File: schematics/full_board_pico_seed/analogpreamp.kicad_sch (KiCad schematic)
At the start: 61 parts, among them J1 XLR3, J3 Aux In, J4 Conn_01x02_Pin, J7 XLR3, J8 XLR3, U1 TL074, U4 NE5534, U9 TL074

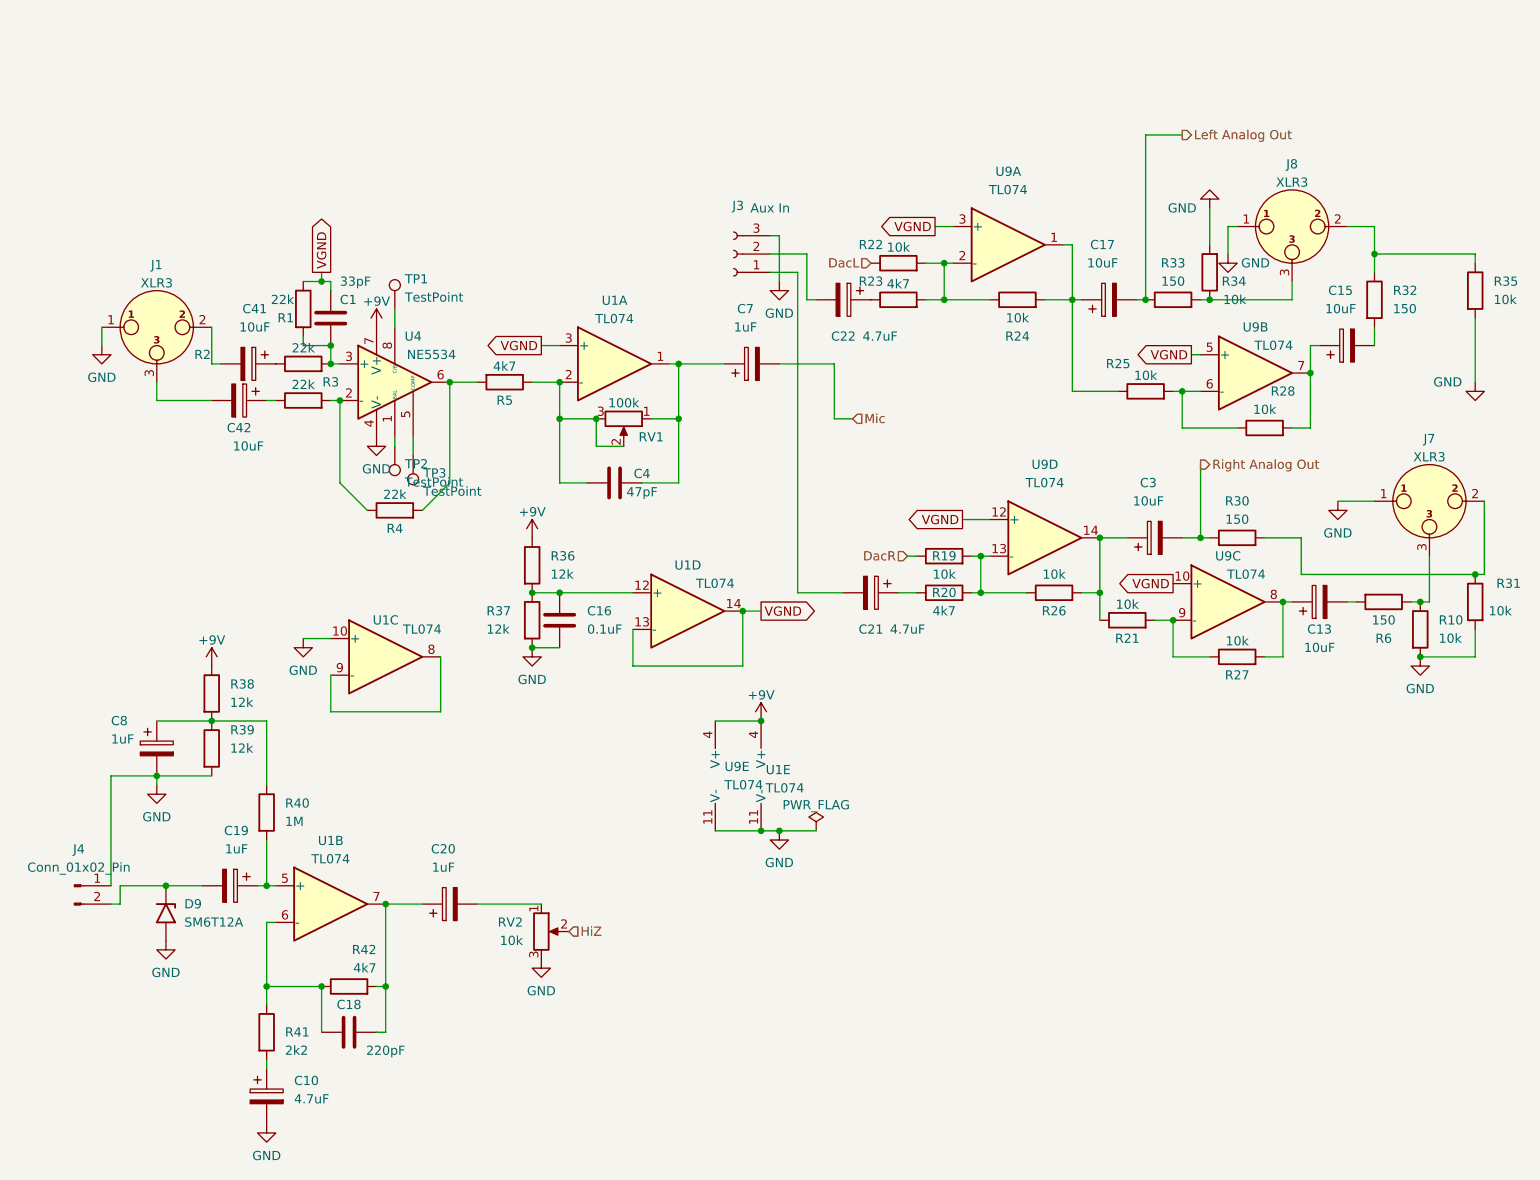
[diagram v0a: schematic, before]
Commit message: more work on full schematic: added test points
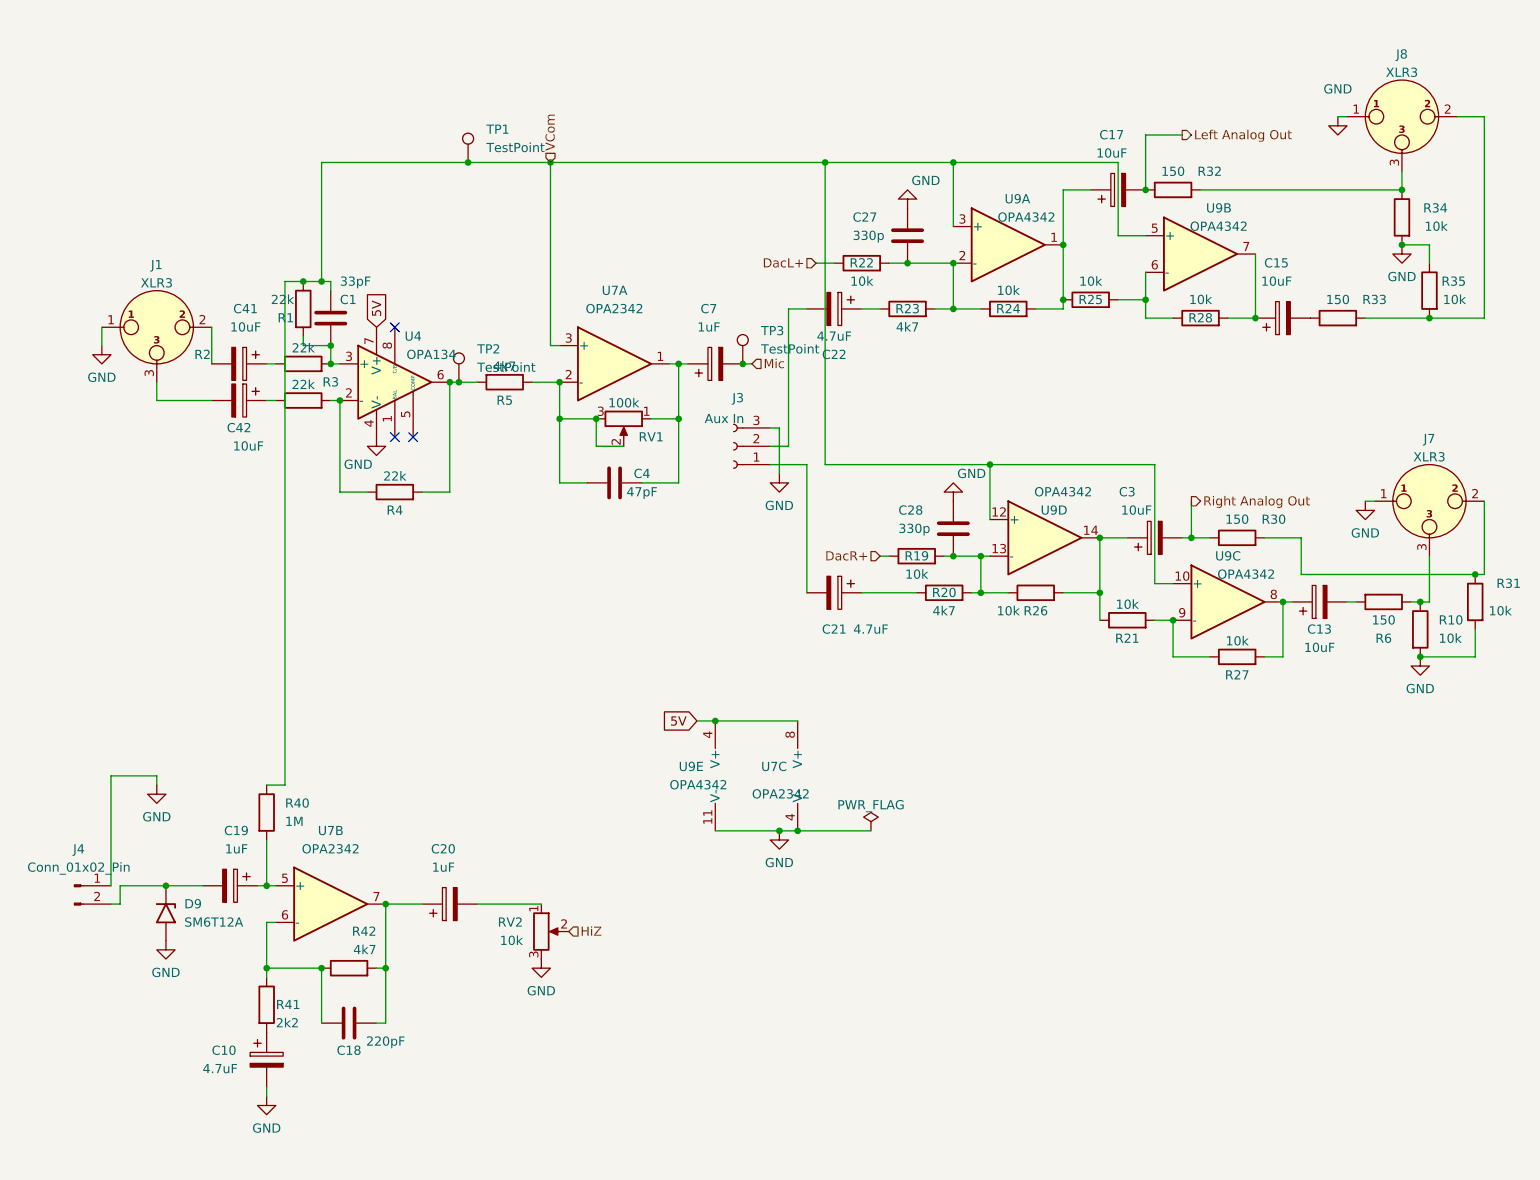
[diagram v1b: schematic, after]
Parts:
- removed C16: 0.1uF, Capacitor_SMD:C_1210_3225Metric_Pad1.33x2.70mm_HandSolder, symbol Device:C
- removed C8: 1uF, Capacitor_SMD:CP_Elec_4x4.5, symbol Device:C_Polarized
- removed R36, R37, R38, R39: 12k, Resistor_SMD:R_0603_1608Metric_Pad0.98x0.95mm_HandSolder, symbol Device:R
- removed U1: TL074, Package_SO:SOIC-14_3.9x8.7mm_P1.27mm, symbol Amplifier_Operational:TL074
- added C27, C28: 330p, Capacitor_SMD:C_0603_1608Metric_Pad1.08x0.95mm_HandSolder, symbol Device:C
- added U7: OPA2342, Package_SO:SOIC-8_3.9x4.9mm_P1.27mm, symbol Amplifier_Operational:TL072
- U4: value NE5534 -> OPA134
- U9: value TL074 -> OPA4342
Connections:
- net VGND is gone; now on net VCom: C1.1, R1.1, U9.10 (+), U9.12 (+), U9.3 (+), U9.5 (+)
- net GND: now also R35.1, C27.1, C28.1, U7.4 (V-); no longer R35.2
- net Left Analog Out: now also R32.1; no longer R33.1
- net Mic: now also TP3.1
- net at U4.1 (BAL): no longer TP2.1
- net at U4.5 (COMP): no longer TP3.1
- net at R4.2, R5.2, U4.6: now also TP2.1
- net at U4.8 (C/B): no longer TP1.1
- net at R19.2, R20.2, R26.1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: now also C28.2
- net at J8.3, R34.1: now also R32.2; no longer R33.2
- net at C4.2, C7.1, RV1.1: now also U7.1
- net at R22.2, R23.2, R24.1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: now also C27.2
- net at C4.1, R5.1, RV1.2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: now also U7.2 (-)
- net at C15.2: now also R33.1; no longer R32.2
- net VCom: now reaches R40.1
- net VCom: now also TP1.1, U7.3 (+)
- net at C18.1, R41.1, R42.1: now also U7.6 (-)
- net at C19.1, R40.2: now also U7.5 (+)
- net at C18.2, C20.1, R42.2: now also U7.7
- net +9V renamed 5V
- net 5V: now also U7.8 (V+)
- net DacL renamed DacL+
- net DacR renamed DacR+
- new net: J8.2, R33.2, R35.2
- no-connect marks 0 -> 3
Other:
- moved on the sheet: C10, C17, C18, C21, C22, C41, C7, J3, J8, R19, R26, R4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

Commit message: worked on schematics
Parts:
- J1, J3, J4, J7, J8, RV1, RV2, TP1, TP2, TP3: now left out of the parts list
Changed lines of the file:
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@@
 		(shape input)
 		(at 88.9 34.29 90)
-		(fields_autoplaced yes)
 		(effects
 			(font
@@
 		(shape input)
 		(at 134.62 88.9 180)
-		(fields_autoplaced yes)
 		(effects
 			(font
@@
 		(shape input)
 		(at 116.84 62.23 0)
-		(fields_autoplaced yes)
 		(effects
 			(font
@@
 		(shape input)
 		(at 125.73 48.26 180)
-		(fields_autoplaced yes)
 		(effects
 			(font
@@
 		(shape output)
 		(at 177.8 81.28 0)
-		(fields_autoplaced yes)
 		(effects
 			(font
@@
 		(shape output)
 		(at 176.53 30.48 0)
-		(fields_autoplaced yes)
 		(effects
 			(font
@@
 		(shape input)
 		(at 91.44 140.97 0)
-		(fields_autoplaced yes)
 		(effects
 			(font
@@
 		(unit 1)
 		(exclude_from_sim no)
-		(in_bom yes)
+		(in_bom no)
 		(on_board yes)
 		(dnp no)
@@
 			)
 		)
-		(property "Datasheet" " ~"
+		(property "Datasheet" "~"
 			(at 34.29 57.15 0)
 			(effects
@@
 		(unit 1)
 		(exclude_from_sim no)
-		(in_bom yes)
+		(in_bom no)
 		(on_board yes)
 		(dnp no)
@@
 			)
 		)
-		(property "Datasheet" " ~"
+		(property "Datasheet" "~"
 			(at 207.01 27.94 0)
 			(effects
@@
 		(unit 1)
 		(exclude_from_sim no)
-		(in_bom yes)
+		(in_bom no)
 		(on_board yes)
 		(dnp no)
@@
 		(unit 1)
 		(exclude_from_sim no)
-		(in_bom yes)
+		(in_bom no)
 		(on_board yes)
 		(dnp no)
@@
 		(unit 1)
 		(exclude_from_sim no)
-		(in_bom yes)
+		(in_bom no)
 		(on_board yes)
 		(dnp no)
@@
 			)
 		)
-		(property "Datasheet" " ~"
+		(property "Datasheet" "~"
 			(at 210.82 81.28 0)
 			(effects
@@
 		(unit 1)
 		(exclude_from_sim no)
-		(in_bom yes)
+		(in_bom no)
 		(on_board yes)
 		(dnp no)
@@
 		(unit 1)
 		(exclude_from_sim no)
-		(in_bom yes)
+		(in_bom no)
 		(on_board yes)
 		(dnp no)
@@
 		(unit 1)
 		(exclude_from_sim no)
-		(in_bom yes)
+		(in_bom no)
 		(on_board yes)
 		(dnp no)
@@
 		(unit 1)
 		(exclude_from_sim no)
-		(in_bom yes)
+		(in_bom no)
 		(on_board yes)
 		(dnp no)
@@
 		(unit 1)
 		(exclude_from_sim no)
-		(in_bom yes)
+		(in_bom no)
 		(on_board yes)
 		(dnp no)

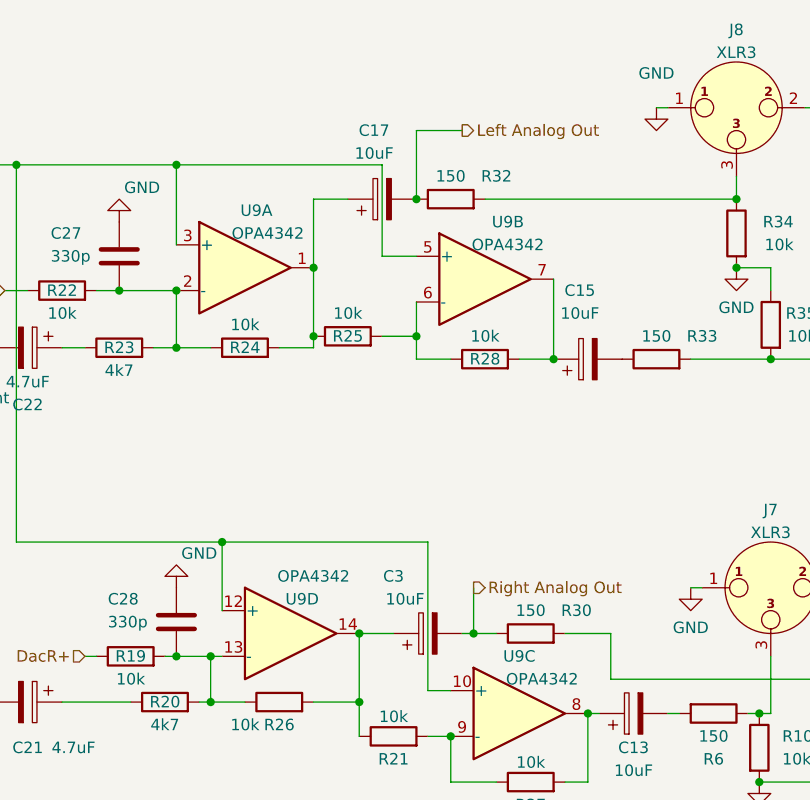
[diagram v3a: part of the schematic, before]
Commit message: corrected wiring mistake found during hw test of first batch
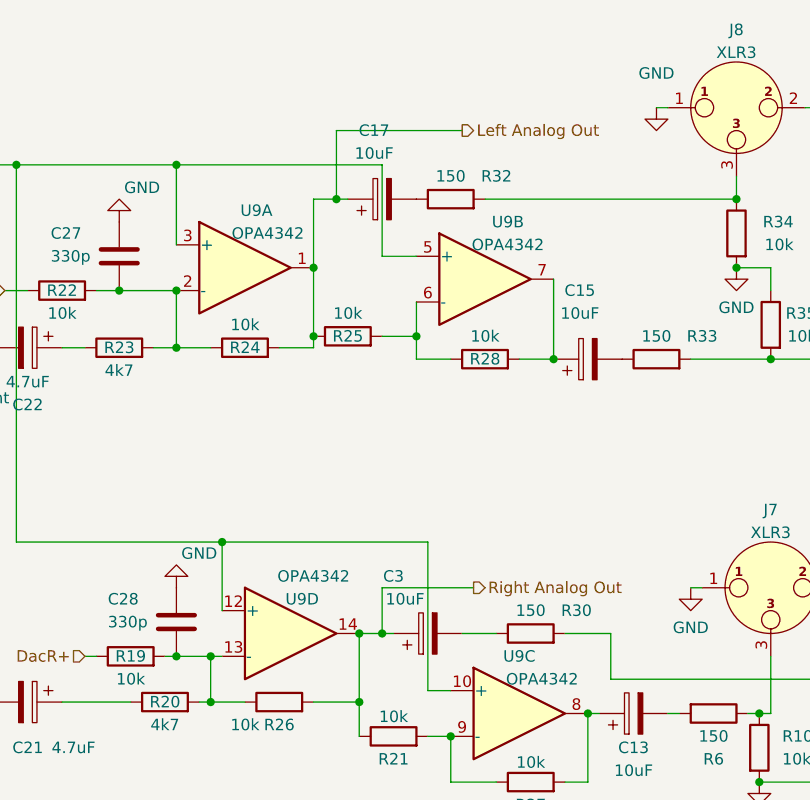
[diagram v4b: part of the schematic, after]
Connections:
- net Left Analog Out: now also C17.1, R24.2, R25.1, U9.1; no longer C17.2, R32.1
- net Right Analog Out: now also C3.1, R21.1, R26.2, U9.14; no longer C3.2, R30.1
- new net: C17.2, R32.1
- new net: C3.2, R30.1
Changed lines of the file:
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@@
+	)
+	(junction
+		(at 162.56 38.1)
+		(diameter 0)
+		(color 0 0 0 0)
 	)
 	(junction
@@
 	)
 	(junction
+		(at 167.64 86.36)
+		(diameter 0)
+		(color 0 0 0 0)
+	)
+	(junction
 		(at 165.1 93.98)
 		(diameter 0)
@@
 	)
 	(junction
-		(at 171.45 38.1)
-		(diameter 0)
-		(color 0 0 0 0)
-	)
-	(junction
 		(at 88.9 34.29)
 		(diameter 0)
@@
 	(junction
 		(at 207.01 45.72)
-		(diameter 0)
-		(color 0 0 0 0)
-	)
-	(junction
-		(at 177.8 86.36)
 		(diameter 0)
 		(color 0 0 0 0)
@@
 	(wire
 		(pts
-			(xy 163.83 38.1) (xy 160.02 38.1)
+			(xy 163.83 38.1) (xy 162.56 38.1)
 		)
 		(stroke
@@
 	(wire
 		(pts
+			(xy 162.56 38.1) (xy 160.02 38.1)
+		)
+		(stroke
+			(width 0)
+			(type default)
+		)
+	)
+	(wire
+		(pts
 			(xy 58.42 52.07) (xy 58.42 50.8)
 		)
@@
 	(wire
 		(pts
-			(xy 165.1 86.36) (xy 168.91 86.36)
+			(xy 165.1 86.36) (xy 167.64 86.36)
 		)
 		(stroke
@@
 	(wire
 		(pts
+			(xy 176.53 30.48) (xy 162.56 30.48)
+		)
+		(stroke
+			(width 0)
+			(type default)
+		)
+	)
+	(wire
+		(pts
 			(xy 54.61 59.69) (xy 58.42 59.69)
 		)
@@
 	(wire
 		(pts
+			(xy 162.56 30.48) (xy 162.56 38.1)
+		)
+		(stroke
+			(width 0)
+			(type default)
+		)
+	)
+	(wire
+		(pts
 			(xy 218.44 27.94) (xy 218.44 55.88)
 		)
@@
 	(wire
 		(pts
-			(xy 171.45 30.48) (xy 176.53 30.48)
-		)
-		(stroke
-			(width 0)
-			(type default)
-		)
-	)
-	(wire
-		(pts
 			(xy 160.02 38.1) (xy 160.02 45.72)
 		)
@@
 	(wire
 		(pts
-			(xy 176.53 86.36) (xy 177.8 86.36)
+			(xy 176.53 86.36) (xy 180.34 86.36)
 		)
 		(stroke
@@
 	(wire
 		(pts
+			(xy 167.64 81.28) (xy 167.64 86.36)
+		)
+		(stroke
+			(width 0)
+			(type default)
+		)
+	)
+	(wire
+		(pts
 			(xy 217.17 91.44) (xy 218.44 91.44)
 		)
@@
 	(wire
 		(pts
-			(xy 171.45 30.48) (xy 171.45 38.1)
-		)
-		(stroke
-			(width 0)
-			(type default)
-		)
-	)
-	(wire
-		(pts
 			(xy 52.07 50.8) (xy 52.07 120.65)
 		)
@@
 	(wire
 		(pts
-			(xy 177.8 81.28) (xy 177.8 86.36)
-		)
-		(stroke
-			(width 0)
-			(type default)
-		)
-	)
-	(wire
-		(pts
 			(xy 26.67 57.15) (xy 26.67 59.69)
 		)
@@
 	(wire
 		(pts
+			(xy 167.64 86.36) (xy 168.91 86.36)
+		)
+		(stroke
+			(width 0)
+			(type default)
+		)
+	)
+	(wire
+		(pts
 			(xy 217.17 102.87) (xy 209.55 102.87)
 		)
@@
 	(wire
 		(pts
-			(xy 177.8 86.36) (xy 180.34 86.36)
-		)
-		(stroke
+			(xy 177.8 81.28) (xy 167.64 81.28)
+		)
+		(stroke
